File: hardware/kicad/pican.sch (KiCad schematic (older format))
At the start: 13 parts, among them P1 CONN_01X06, P2 CONN_01X03, U1 MCP2515, U2 MCP2562, Y1 16MHz

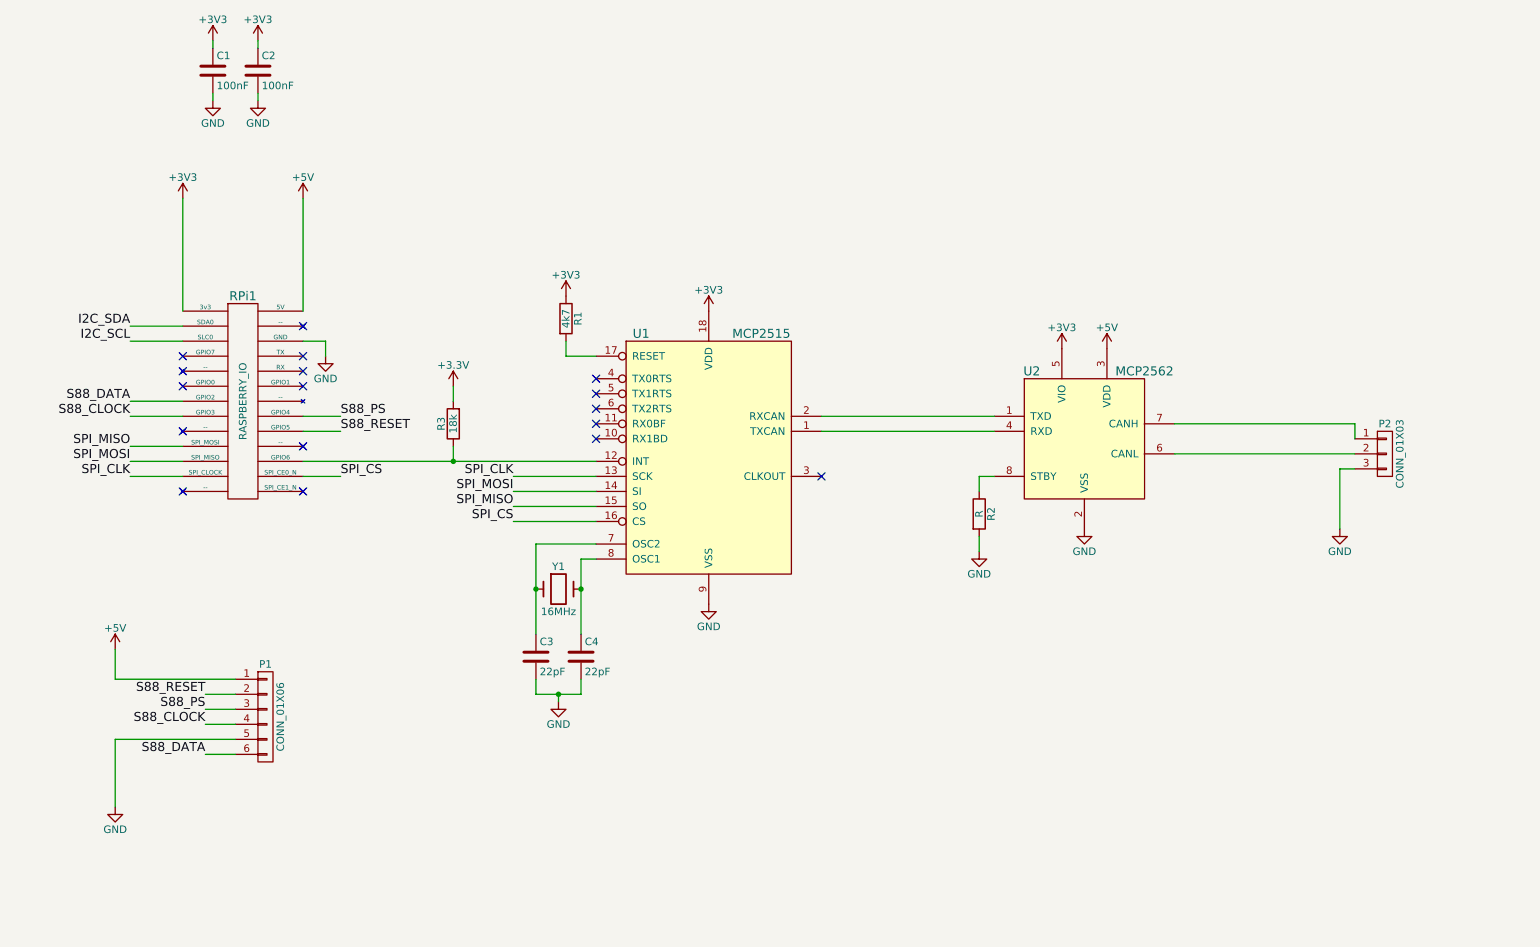
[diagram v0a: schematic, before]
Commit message: Add optocoupler and started new PCB.
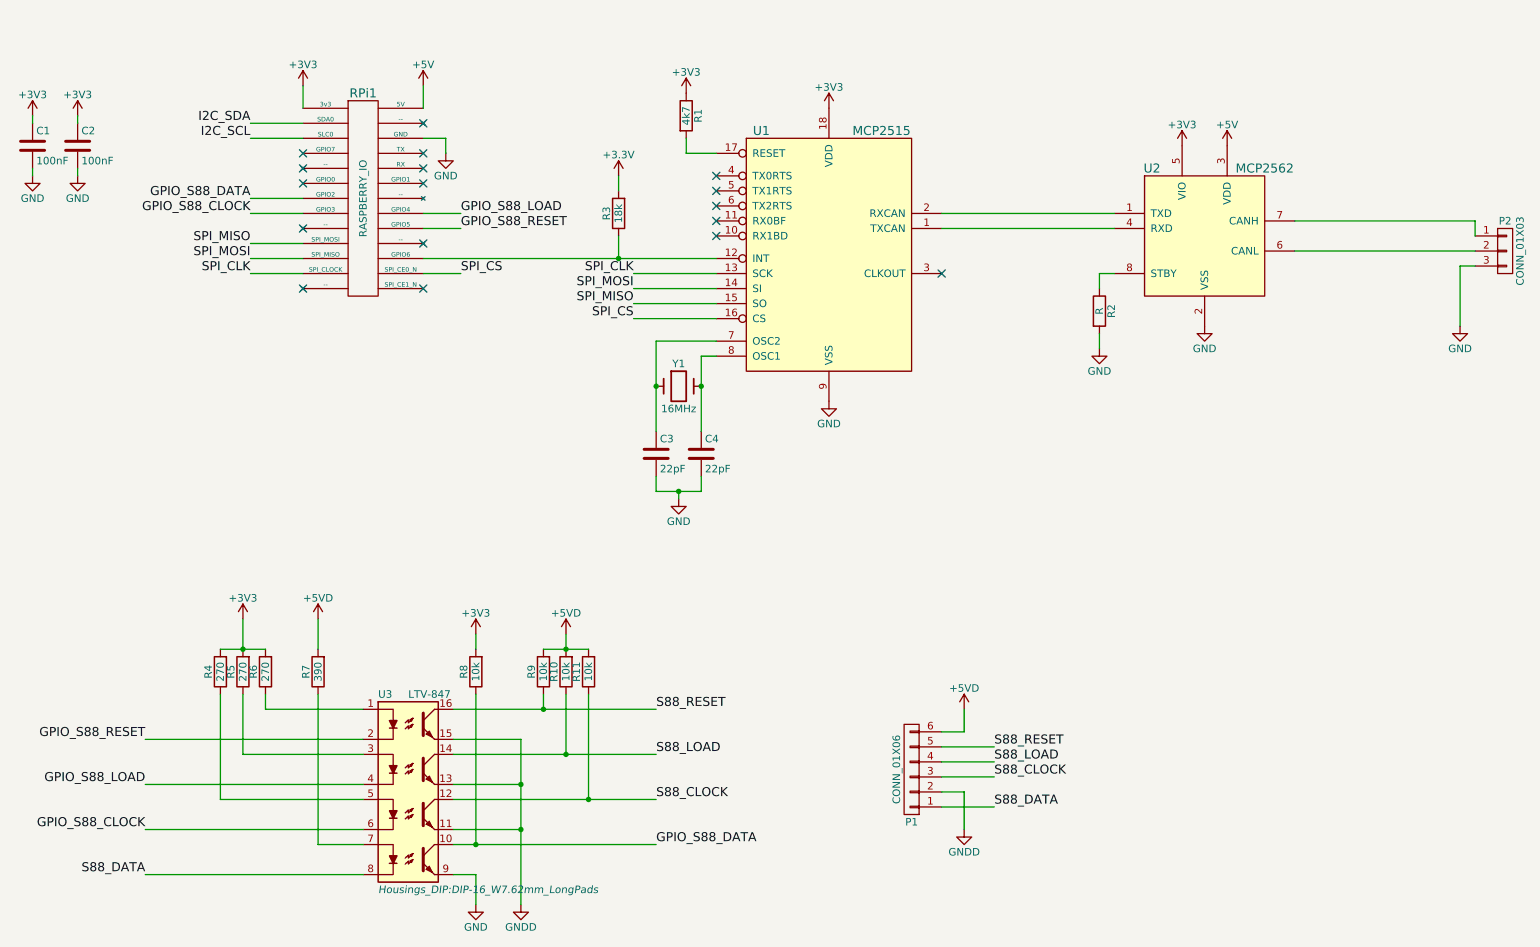
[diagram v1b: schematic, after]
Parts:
- added R10, R11, R8, R9: 10k, Resistors_ThroughHole:Resistor_Horizontal_RM10mm, symbol R
- added R4, R5, R6: 270, Resistors_ThroughHole:Resistor_Horizontal_RM10mm, symbol R
- added R7: 390, Resistors_ThroughHole:Resistor_Horizontal_RM10mm, symbol R
- added U3: LTV-847, Housings_DIP:DIP-16_W7.62mm_LongPads, symbol LTV-847
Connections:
- net +3V3: now also R4.2, R5.2, R6.2, R8.2
- net +5V: no longer P1.1 (P1)
- net GND: now also U3.9; no longer P1.5 (P5)
- net S88_CLOCK: now also P1.3 (P3), R11.1, U3.12; no longer P1.4 (P4), RPi1.15 (GPIO3)
- net S88_DATA: now also P1.1 (P1), U3.8; no longer P1.6 (P6), RPi1.13 (GPIO2)
- net S88_RESET: now also P1.5 (P5), R9.1, U3.16; no longer P1.2 (P2), RPi1.18 (GPIO5)
- net S88_PS renamed GPIO_S88_LOAD
- net GPIO_S88_LOAD: now also U3.4; no longer P1.3 (P3)
- new net: R6.1, U3.1
- new net: R5.1, U3.3
- new net: R4.1, U3.5
- new net: R7.1, U3.7
- new net +5VD: P1.6 (P6), R10.2, R11.2, R7.2, R9.2
- new net GNDD: P1.2 (P2), U3.11, U3.13, U3.15
- new net GPIO_S88_CLOCK: RPi1.15 (GPIO3), U3.6
- new net GPIO_S88_DATA: R8.1, RPi1.13 (GPIO2), U3.10
- new net GPIO_S88_RESET: RPi1.18 (GPIO5), U3.2
- new net S88_LOAD: P1.4 (P4), R10.1, U3.14
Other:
- moved on the sheet: C1, C2, C3, C4, P1, P2, R1, R2, R3, RPi1, U1, U2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

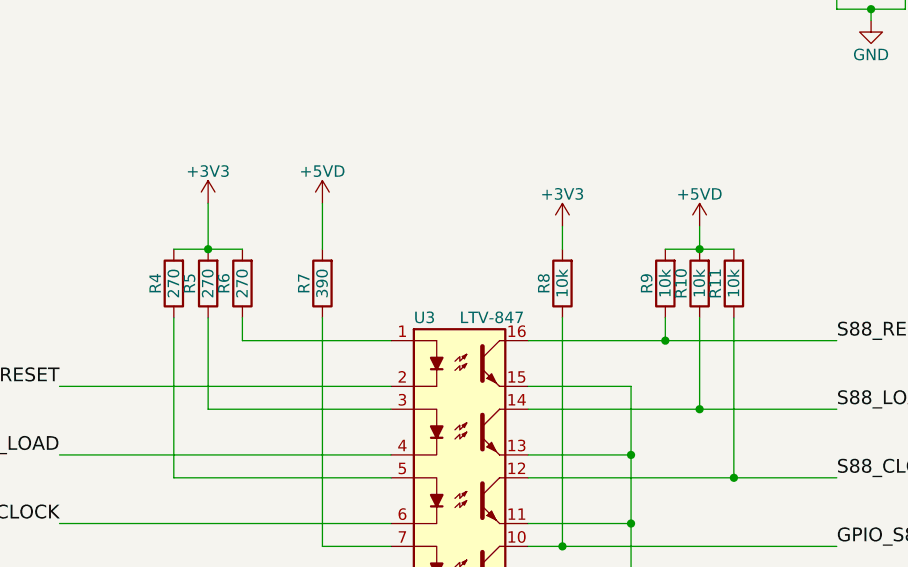
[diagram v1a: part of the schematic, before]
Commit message: change resistor values for optocoupler
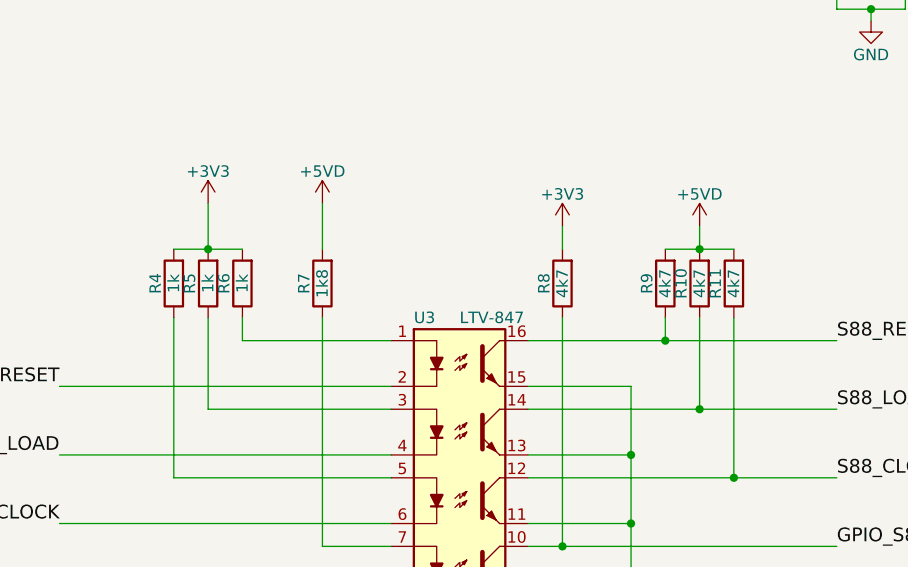
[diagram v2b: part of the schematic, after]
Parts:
- R10, R11, R8, R9: value 10k -> 4k7
- R4, R5, R6: value 270 -> 1k
- R7: value 390 -> 1k8
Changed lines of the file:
@@
 P 2750 5050
 F 0 "R7" V 2830 5050 50  0000 C CNN
-F 1 "390" V 2750 5050 50  0000 C CNN
+F 1 "1k8" V 2750 5050 50  0000 C CNN
 F 2 "Resistors_ThroughHole:Resistor_Horizontal_RM10mm" V 2850 5050 50  0001 C CNN
 F 3 "" H 2750 5050 50  0000 C CNN
@@
 P 2400 5050
 F 0 "R6" V 2480 5050 50  0000 C CNN
-F 1 "270" V 2400 5050 50  0000 C CNN
+F 1 "1k" V 2400 5050 50  0000 C CNN
 F 2 "Resistors_ThroughHole:Resistor_Horizontal_RM10mm" V 2500 5050 50  0001 C CNN
 F 3 "" H 2400 5050 50  0000 C CNN
@@
 P 2250 5050
 F 0 "R5" V 2330 5050 50  0000 C CNN
-F 1 "270" V 2250 5050 50  0000 C CNN
+F 1 "1k" V 2250 5050 50  0000 C CNN
 F 2 "Resistors_ThroughHole:Resistor_Horizontal_RM10mm" V 2350 5050 50  0001 C CNN
 F 3 "" H 2250 5050 50  0000 C CNN
@@
 P 2100 5050
 F 0 "R4" V 2180 5050 50  0000 C CNN
-F 1 "270" V 2100 5050 50  0000 C CNN
+F 1 "1k" V 2100 5050 50  0000 C CNN
 F 2 "Resistors_ThroughHole:Resistor_Horizontal_RM10mm" V 2200 5050 50  0001 C CNN
 F 3 "" H 2100 5050 50  0000 C CNN
@@
 P 3800 5050
 F 0 "R8" V 3880 5050 50  0000 C CNN
-F 1 "10k" V 3800 5050 50  0000 C CNN
+F 1 "4k7" V 3800 5050 50  0000 C CNN
 F 2 "Resistors_ThroughHole:Resistor_Horizontal_RM10mm" V 3900 5050 50  0001 C CNN
 F 3 "" H 3800 5050 50  0000 C CNN
@@
 P 4250 5050
 F 0 "R9" V 4330 5050 50  0000 C CNN
-F 1 "10k" V 4250 5050 50  0000 C CNN
+F 1 "4k7" V 4250 5050 50  0000 C CNN
 F 2 "Resistors_ThroughHole:Resistor_Horizontal_RM10mm" V 4350 5050 50  0001 C CNN
 F 3 "" H 4250 5050 50  0000 C CNN
@@
 P 4400 5050
 F 0 "R10" V 4480 5050 50  0000 C CNN
-F 1 "10k" V 4400 5050 50  0000 C CNN
+F 1 "4k7" V 4400 5050 50  0000 C CNN
 F 2 "Resistors_ThroughHole:Resistor_Horizontal_RM10mm" V 4500 5050 50  0001 C CNN
 F 3 "" H 4400 5050 50  0000 C CNN
@@
 P 4550 5050
 F 0 "R11" V 4630 5050 50  0000 C CNN
-F 1 "10k" V 4550 5050 50  0000 C CNN
+F 1 "4k7" V 4550 5050 50  0000 C CNN
 F 2 "Resistors_ThroughHole:Resistor_Horizontal_RM10mm" V 4650 5050 50  0001 C CNN
 F 3 "" H 4550 5050 50  0000 C CNN
